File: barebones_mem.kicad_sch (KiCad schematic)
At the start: 12 parts, among them Q4 MMBT3904, U30 W25Q256JWEIQ, U31 PCF85063ATL/1,118

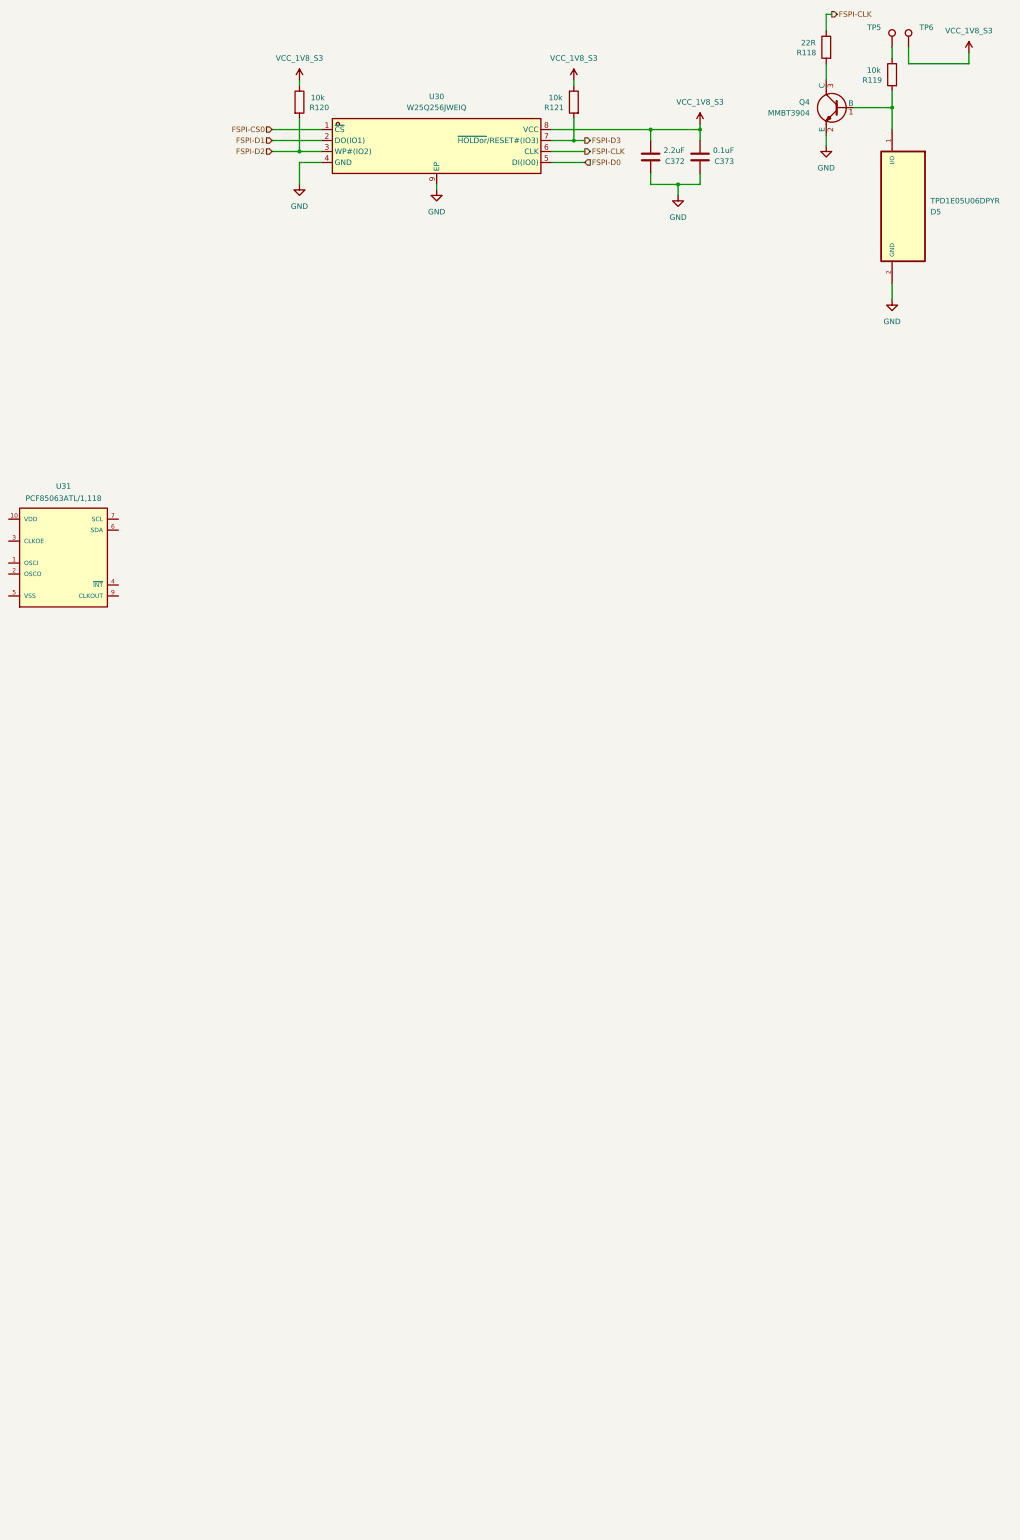
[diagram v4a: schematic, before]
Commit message: added the PCF85063ATL/1,118 CMOS Real-Time Clock
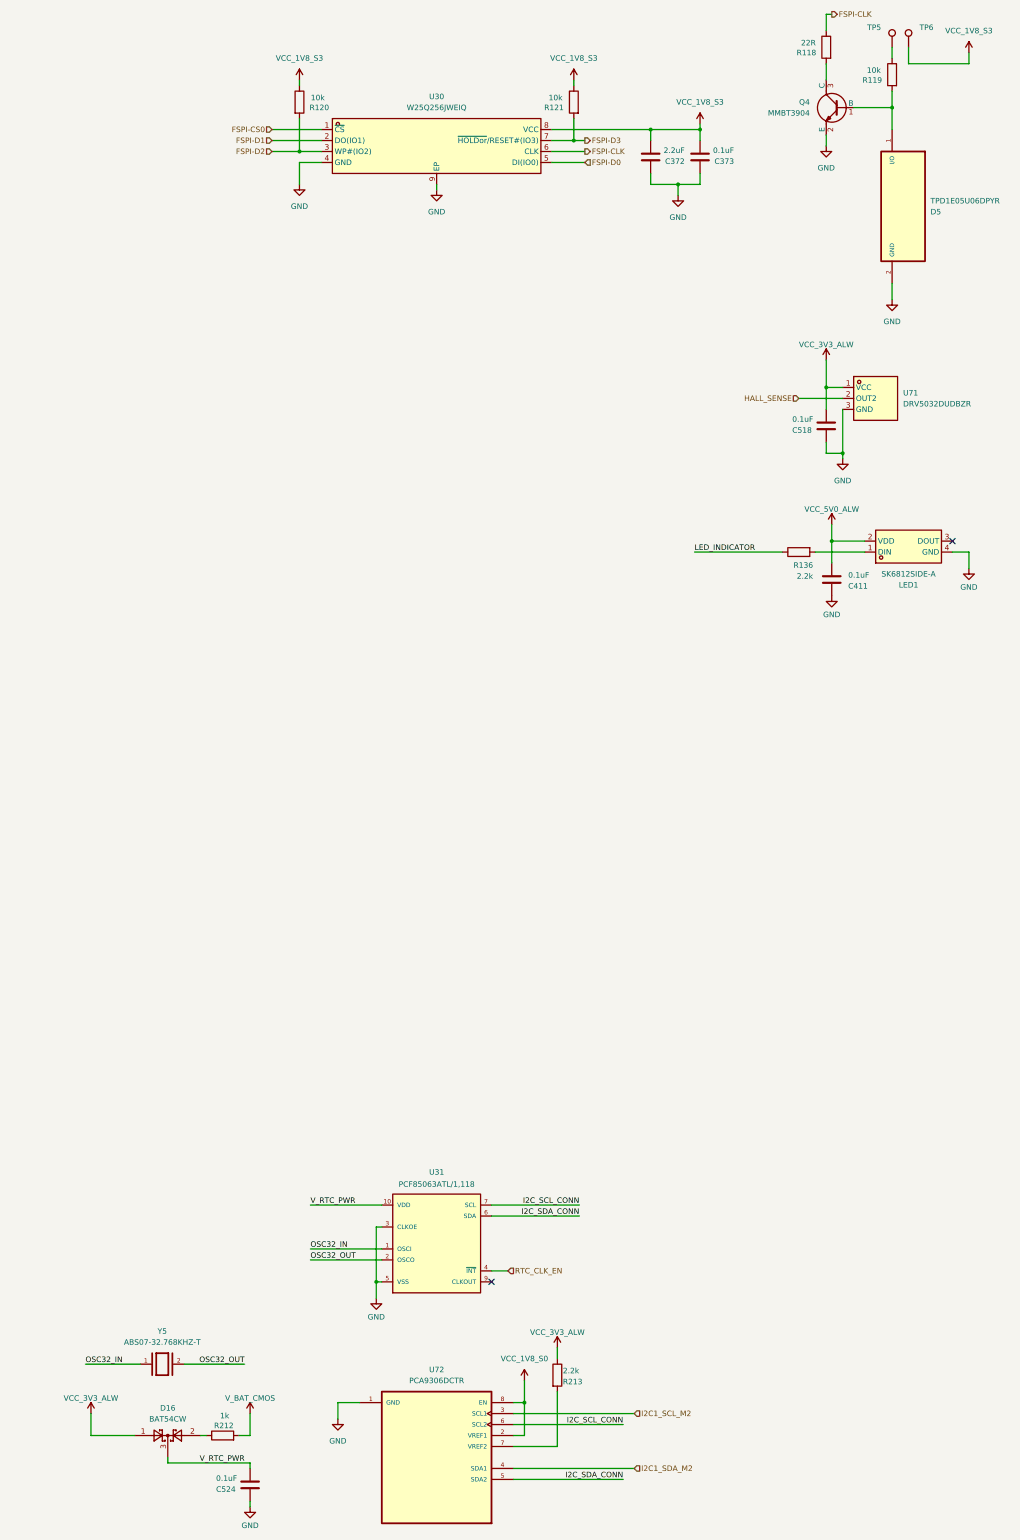
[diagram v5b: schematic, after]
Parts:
- added C411, C518, C524: 0.1uF, Capacitor_SMD:C_0603_1608Metric, symbol Device:C
- added D16: BAT54CW, Package_TO_SOT_SMD:SOT-323_SC-70, symbol Diode:BAT54CW
- added LED1: SK6812SIDE-A, easyeda2kicad:LED-SMD_4P-L4.0-W1.6-L, symbol SK6812_SIDE-A:SK6812SIDE-A_C5378721
- added R136: 2.2k, Resistor_SMD:R_0603_1608Metric, symbol Device:R
- added R212: 1k, Resistor_SMD:R_0603_1608Metric, symbol Device:R
- added R213: 2.2k, Resistor_SMD:R_0402_1005Metric, symbol Device:R
- added U71: DRV5032DUDBZR, easyeda2kicad:SOT-23-3_L2.9-W1.3-P1.90-LS2.4-BR, symbol DRV5032DUDBZR:DRV5032DUDBZR
- added U72: PCA9306DCTR, barebones:SOP65P400X130-8N, symbol PCA9306DCTR:PCA9306DCTR
- added Y5: ABS07-32.768KHZ-T, ABS07-32.768KHZ-T:XTAL_ABS07-32.768KHZ-T, symbol ABS07-32.768KHZ-T:ABS07-32.768KHZ-T
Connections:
- net VSS is gone; now on net GND: U31.11 (VSS), U31.5 (VSS)
- net GND: now also U31.3 (CLKOE), C411.2, C518.1, C524.1, LED1.4 (GND), U71.3 (GND), U72.1 (GND)
- net OSC32_IN: now reaches U31.1 (OSCI)
- net OSC32_IN: now also Y5.1
- net V_RTC_PWR: now reaches U31.10 (VDD)
- net V_RTC_PWR: now also C524.2, D16.3
- net OSC32_OUT: now reaches U31.2 (OSCO)
- net OSC32_OUT: now also Y5.2
- net RTC_CLK_EN: now reaches U31.4 (~{INT})
- net I2C_SDA_CONN: now reaches U31.6 (SDA)
- net I2C_SDA_CONN: now also U72.5 (SDA2)
- net I2C_SCL_CONN: now reaches U31.7 (SCL)
- net I2C_SCL_CONN: now also U72.6 (SCL2)
- new net: D16.2, R212.1
- new net: LED1.1 (DIN), R136.2
- new net: R213.2, U72.7 (VREF2)
- new net HALL_SENSE: U71.2 (OUT2)
- new net I2C1_SCL_M2: U72.3 (SCL1)
- new net I2C1_SDA_M2: U72.4 (SDA1)
- new net LED_INDICATOR: R136.1
- new net VCC_1V8_S0: U72.2 (VREF1), U72.8 (EN)
- new net VCC_3V3_ALW: C518.2, D16.1, R213.1, U71.1 (VCC)
- new net VCC_5V0_ALW: C411.1, LED1.2 (VDD)
- new net V_BAT_CMOS: R212.2
- no-connect marks 0 -> 2
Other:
- moved on the sheet: U31
